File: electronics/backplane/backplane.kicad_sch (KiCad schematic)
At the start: 0 parts

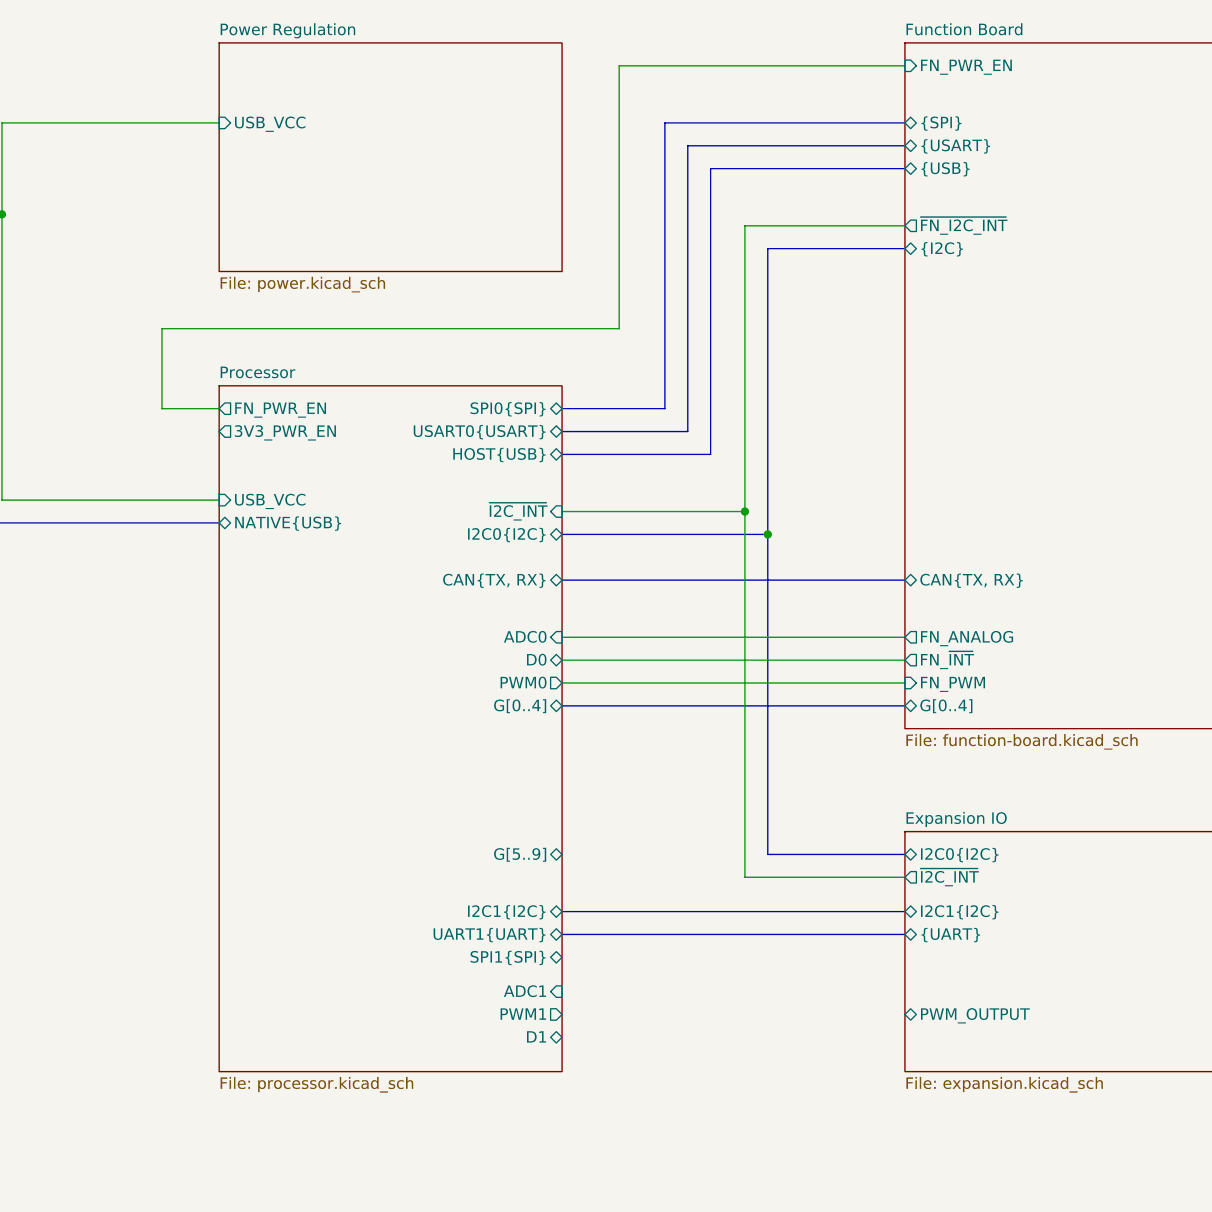
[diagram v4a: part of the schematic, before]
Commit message: Continue backplane design Cleanup schematic, most routing and placement done
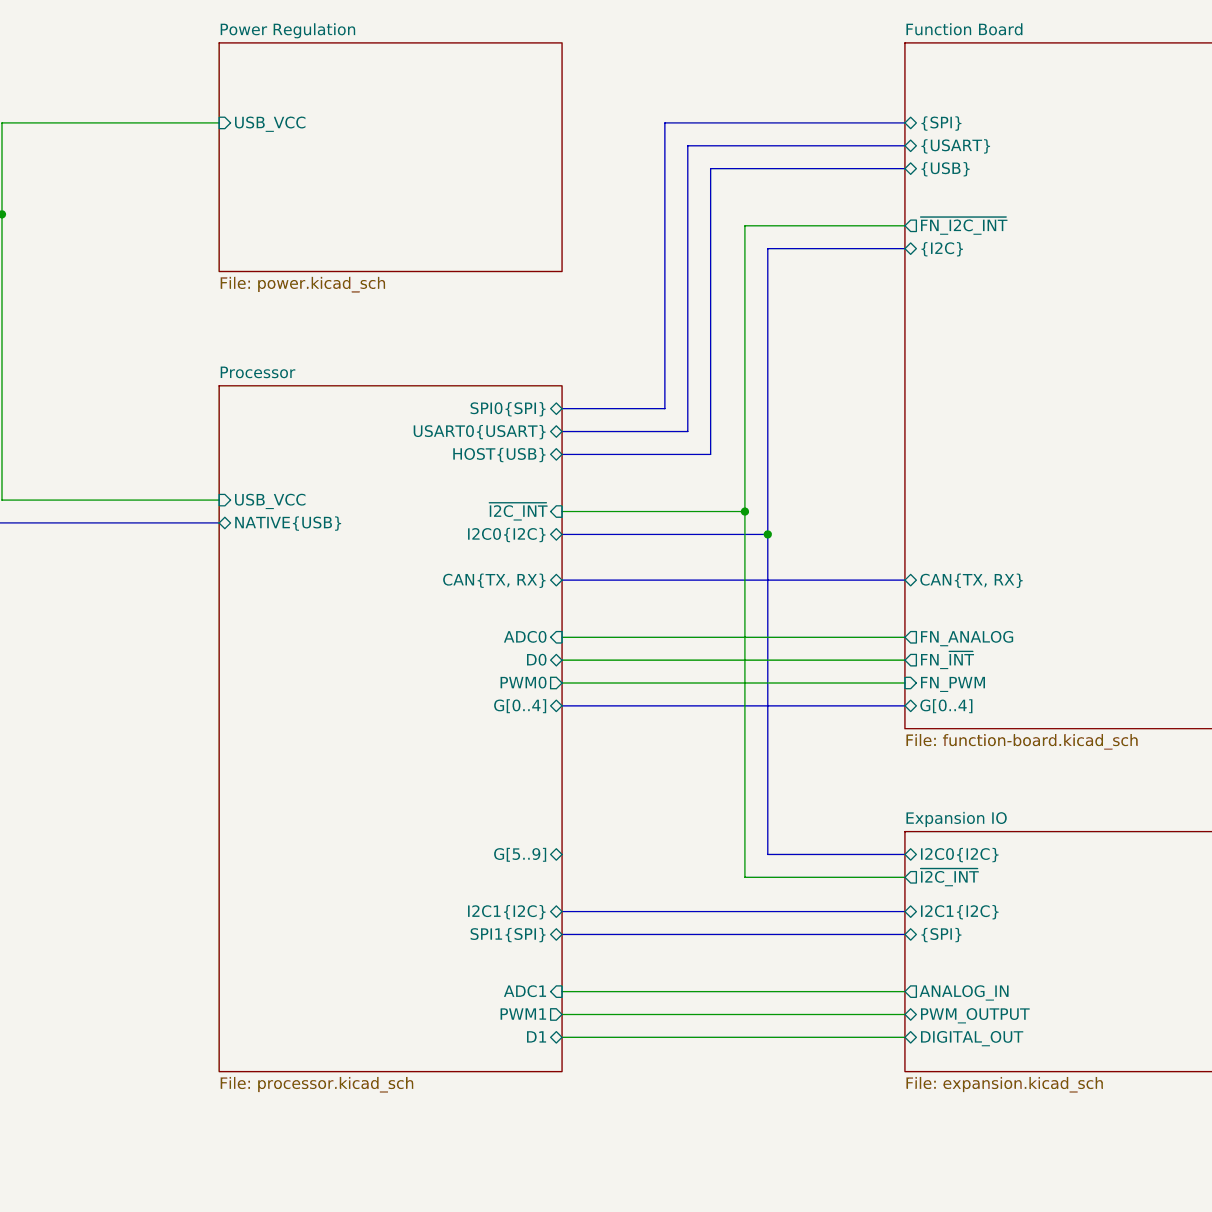
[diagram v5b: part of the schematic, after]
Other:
- sheet Expansion IO ports: added ANALOG_IN, DIGITAL_OUT, {SPI}; removed {UART}
- sheet Function Board ports: added none; removed FN_PWR_EN
- sheet Processor ports: added none; removed 3V3_PWR_EN, FN_PWR_EN, UART1{UART}
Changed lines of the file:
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@@
-    (stroke (width 0) (type default))
-  )
-  (wire (pts (xy 190.5 27.94) (xy 158.75 27.94))
     (stroke (width 0) (type default))
   )
@@
     (stroke (width 0) (type default))
   )
-  (wire (pts (xy 158.75 27.94) (xy 158.75 57.15))
-    (stroke (width 0) (type default))
-  )
   (wire (pts (xy 90.17 44.45) (xy 90.17 76.2))
     (stroke (width 0) (type default))
@@
     (stroke (width 0) (type default))
   )
-  (wire (pts (xy 107.95 57.15) (xy 158.75 57.15))
-    (stroke (width 0) (type default))
-  )
   (bus (pts (xy 87.63 78.74) (xy 114.3 78.74))
     (stroke (width 0) (type default))
@@
     (stroke (width 0) (type default))
   )
+  (wire (pts (xy 152.4 130.81) (xy 190.5 130.81))
+    (stroke (width 0) (type default))
+  )
+  (wire (pts (xy 152.4 133.35) (xy 190.5 133.35))
+    (stroke (width 0) (type default))
+  )
   (wire (pts (xy 90.17 34.29) (xy 114.3 34.29))
     (stroke (width 0) (type default))
   )
+  (wire (pts (xy 152.4 96.52) (xy 190.5 96.52))
+    (stroke (width 0) (type default))
+  )
+  (bus (pts (xy 166.37 68.58) (xy 166.37 36.83))
+    (stroke (width 0) (type default))
+  )
+  (wire (pts (xy 90.17 76.2) (xy 114.3 76.2))
+    (stroke (width 0) (type default))
+  )
+  (bus (pts (xy 163.83 66.04) (xy 163.83 34.29))
+    (stroke (width 0) (type default))
+  )
+  (bus (pts (xy 175.26 115.57) (xy 175.26 80.01))
+    (stroke (width 0) (type default))
+  )
+  (wire (pts (xy 172.72 77.47) (xy 172.72 45.72))
+    (stroke (width 0) (type default))
+  )
+  (wire (pts (xy 152.4 135.89) (xy 190.5 135.89))
+    (stroke (width 0) (type default))
+  )
+  (bus (pts (xy 190.5 115.57) (xy 175.26 115.57))
+    (stroke (width 0) (type default))
+  )
+  (bus (pts (xy 152.4 71.12) (xy 168.91 71.12))
+    (stroke (width 0) (type default))
+  )
+  (wire (pts (xy 76.2 44.45) (xy 90.17 44.45))
+    (stroke (width 0) (type default))
+  )
   (bus (pts (xy 152.4 124.46) (xy 190.5 124.46))
-    (stroke (width 0) (type default))
-  )
-  (wire (pts (xy 152.4 96.52) (xy 190.5 96.52))
-    (stroke (width 0) (type default))
-  )
-  (bus (pts (xy 166.37 68.58) (xy 166.37 36.83))
-    (stroke (width 0) (type default))
-  )
-  (wire (pts (xy 90.17 76.2) (xy 114.3 76.2))
-    (stroke (width 0) (type default))
-  )
-  (bus (pts (xy 163.83 66.04) (xy 163.83 34.29))
-    (stroke (width 0) (type default))
-  )
-  (bus (pts (xy 175.26 115.57) (xy 175.26 80.01))
-    (stroke (width 0) (type default))
-  )
-  (wire (pts (xy 172.72 77.47) (xy 172.72 45.72))
-    (stroke (width 0) (type default))
-  )
-  (bus (pts (xy 190.5 115.57) (xy 175.26 115.57))
-    (stroke (width 0) (type default))
-  )
-  (bus (pts (xy 152.4 71.12) (xy 168.91 71.12))
-    (stroke (width 0) (type default))
-  )
-  (wire (pts (xy 76.2 44.45) (xy 90.17 44.45))
-    (stroke (width 0) (type default))
-  )
-  (wire (pts (xy 114.3 66.04) (xy 107.95 66.04))
-    (stroke (width 0) (type default))
-  )
-  (wire (pts (xy 107.95 66.04) (xy 107.95 57.15))
     (stroke (width 0) (type default))
   )
@@
       (effects (font (size 1.27 1.27)) (justify right))
     )
-    (pin "3V3_PWR_EN" output (at 114.3 68.58 180)
-      (effects (font (size 1.27 1.27)) (justify left))
-    )
     (pin "NATIVE{USB}" bidirectional (at 114.3 78.74 180)
       (effects (font (size 1.27 1.27)) (justify left))
@@
       (effects (font (size 1.27 1.27)) (justify right))
     )
-    (pin "UART1{UART}" bidirectional (at 152.4 124.46 0)
-      (effects (font (size 1.27 1.27)) (justify right))
-    )
     (pin "D0" bidirectional (at 152.4 93.98 0)
       (effects (font (size 1.27 1.27)) (justify right))
@@
       (effects (font (size 1.27 1.27)) (justify right))
     )
-    (pin "SPI1{SPI}" bidirectional (at 152.4 127 0)
+    (pin "SPI1{SPI}" bidirectional (at 152.4 124.46 0)
       (effects (font (size 1.27 1.27)) (justify right))
     )
@@
     (pin "ADC1" input (at 152.4 130.81 0)
       (effects (font (size 1.27 1.27)) (justify right))
-    )
-    (pin "FN_PWR_EN" output (at 114.3 66.04 180)
-      (effects (font (size 1.27 1.27)) (justify left))
     )
     (pin "G[5..9]" bidirectional (at 152.4 115.57 0)
@@
       (effects (font (size 1.27 1.27)) (justify left))
     )
-    (pin "FN_PWR_EN" input (at 190.5 27.94 180)
-      (effects (font (size 1.27 1.27)) (justify left))
-    )
     (pin "{SPI}" bidirectional (at 190.5 34.29 180)
       (effects (font (size 1.27 1.27)) (justify left))
@@
       (effects (font (size 1.27 1.27)) (justify left))
     )
-    (pin "{UART}" bidirectional (at 190.5 124.46 180)
-      (effects (font (size 1.27 1.27)) (justify left))
-    )
     (pin "PWM_OUTPUT" bidirectional (at 190.5 133.35 180)
       (effects (font (size 1.27 1.27)) (justify left))
     )
+    (pin "{SPI}" bidirectional (at 190.5 124.46 180)
+      (effects (font (size 1.27 1.27)) (justify left))
+    )
+    (pin "DIGITAL_OUT" bidirectional (at 190.5 135.89 180)
+      (effects (font (size 1.27 1.27)) (justify left))
+    )
+    (pin "ANALOG_IN" output (at 190.5 130.81 180)
+      (effects (font (size 1.27 1.27)) (justify left))
+    )

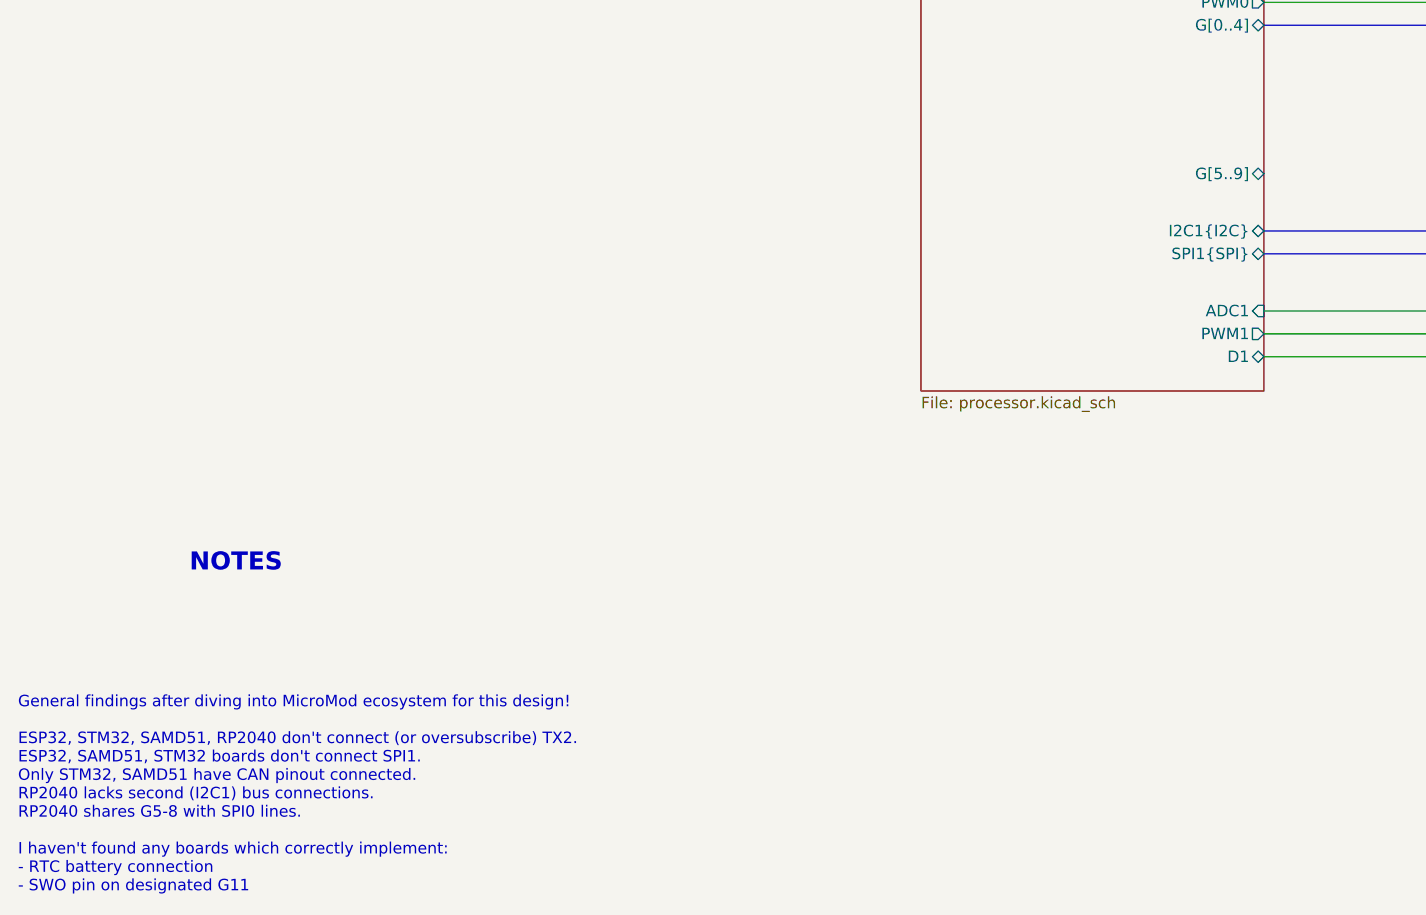
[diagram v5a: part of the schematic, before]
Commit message: Backplane routing complete General schematic cleanup, board cosmetics etc
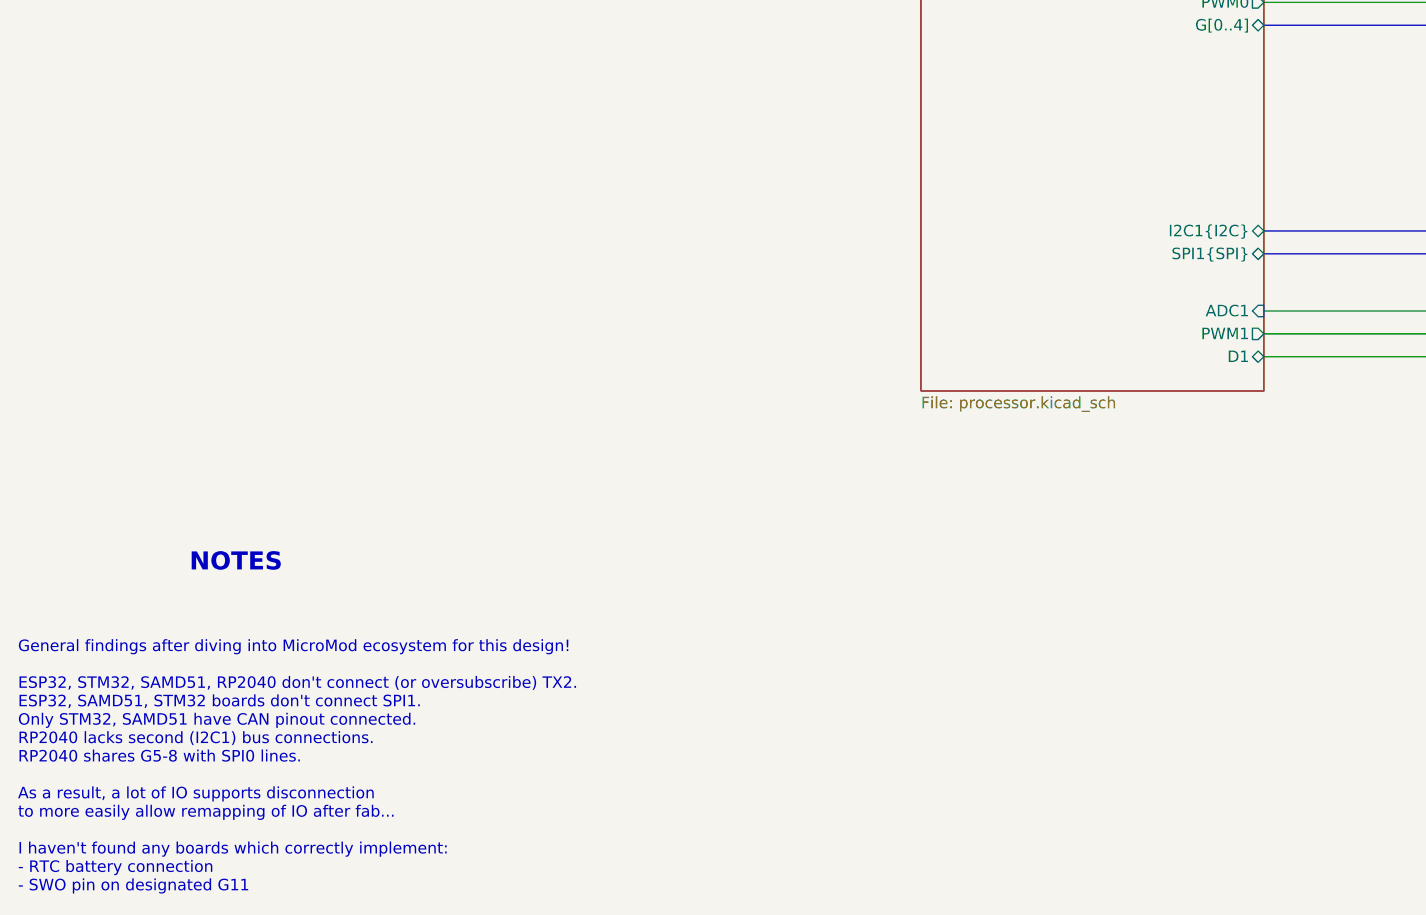
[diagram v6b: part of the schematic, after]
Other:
- sheet Processor ports: added none; removed G[5..9]
- note added: "General findings after diving into MicroMod ecosystem for this design! ESP32, STM32, SAMD51, RP2040 don't connect (or oversubscribe) TX2. ESP32, SAMD51, STM32 boards don't connect SPI1. Only STM32, SAMD51 have CAN pinout connected. RP2040 lacks second (I2C1) bus connections. RP2040 shares G5-8 with SPI0 lines. As a result, a lot of IO supports disconnection to more easily allow remapping of IO af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"
- note removed: "General findings after diving into MicroMod ecosystem for this design! ESP32, STM32, SAMD51, RP2040 don't connect (or oversubscribe) TX2. ESP32, SAMD51, STM32 boards don't connect SPI1. Only STM32, SAMD51 have CAN pinout connected. RP2040 lacks second (I2C1) bus connections. RP2040 shares G5-8 with SPI0 lines. I haven't found any boards which correctly implement: - RTC battery connection - SWO pi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"
- title: (none) -> SPE-NODE-BACKPLANE
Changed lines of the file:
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@@
 (kicad_sch (version 20230121) (generator eeschema)
   (paper "A4")
+  (title_block
+    (title "SPE-NODE-BACKPLANE")
+    (date "2023-08-09")
+    (rev "V1.0")
+  )
   (bus_alias "I2C" (members "SDA" "SCL"))
   (bus_alias "USB" (members "D+" "D-"))
@@
     (effects (font (size 2 2) (thickness 0.4) bold) (justify left bottom))
   )
-  (text "General findings after diving into MicroMod ecosystem for this design!\n\nESP32, STM32, SAMD51, RP2040 don't connect (or oversubscribe) TX2.\nESP32, SAMD51, STM32 boards don't connect SPI1.\nOnly STM32, SAMD51 have CAN pinout connected.\nRP2040 lacks second (I2C1) bus connections.\nRP2040 shares G5-8 with SPI0 lines.\n\nI haven't found any boards which correctly implement:\n- RTC battery connection\n- SWO pin on designated G11"
+  (text "General findings after diving into MicroMod ecosystem for this design!\n\nESP32, STM32, SAMD51, RP2040 don't connect (or oversubscribe) TX2.\nESP32, SAMD51, STM32 boards don't connect SPI1.\nOnly STM32, SAMD51 have CAN pinout connected.\nRP2040 lacks second (I2C1) bus connections.\nRP2040 shares G5-8 with SPI0 lines.\n\nAs a result, a lot of IO supports disconnection \nto more easily allow remapping of IO after fab...\n\nI haven't found any boards which correctly implement:\n- RTC battery connection\n- SWO pin on designated G11"
     (at 13.97 195.58 0)
     (effects (font (size 1.27 1.27)) (justify left bottom))
@@
       (effects (font (size 1.27 1.27)) (justify right))
     )
-    (pin "G[5..9]" bidirectional (at 152.4 115.57 0)
-      (effects (font (size 1.27 1.27)) (justify right))
-    )
